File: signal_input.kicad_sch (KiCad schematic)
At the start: 32 parts, among them IC1 TXU0104QWBQARQ1, IC2 TXU0104QWBQARQ1, IC3 TXU0104QWBQARQ1, IC4 TXU0104QWBQARQ1, J4 6101XX249121_610108249121, J5 6101XX249121_610108249121, J6 6101XX249121_610108249121, J7 6101XX249121_610108249121

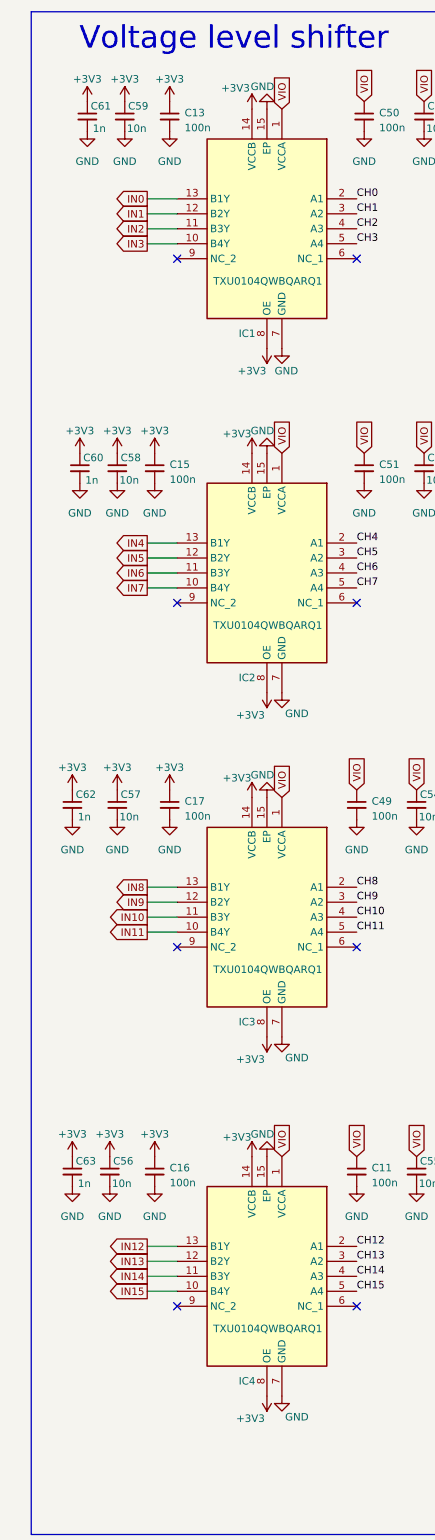
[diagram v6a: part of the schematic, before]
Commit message: implement USB3.0 active redriver and fix DRC errors
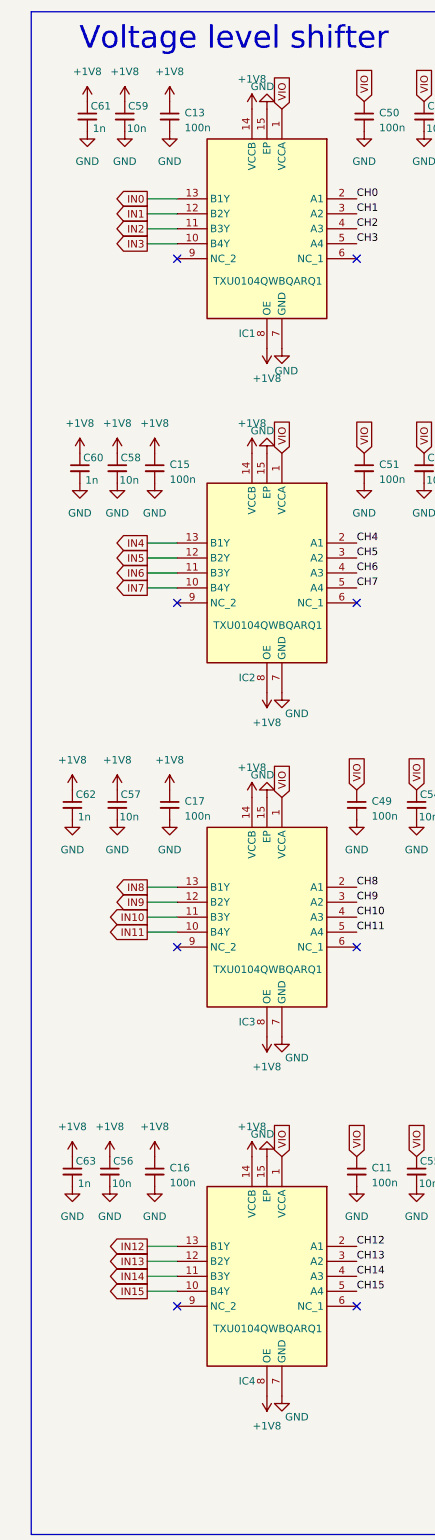
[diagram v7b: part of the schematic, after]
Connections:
- net +3V3 renamed +1V8
